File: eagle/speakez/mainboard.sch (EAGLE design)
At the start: 39 parts, among them U1 +12v

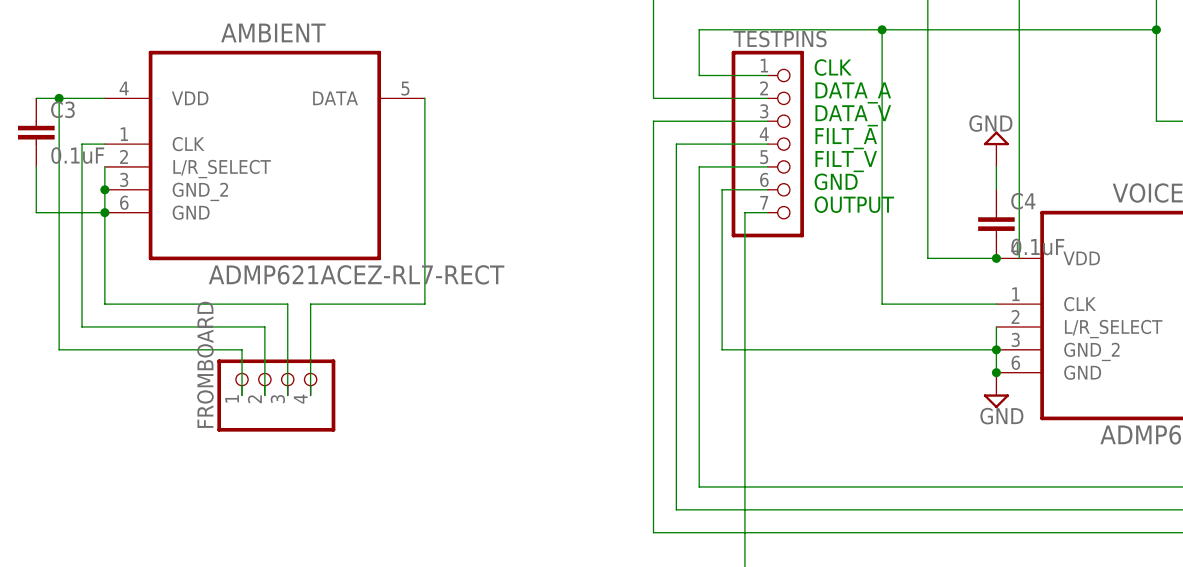
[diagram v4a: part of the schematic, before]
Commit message: started working on removing overlaps/clearance issues
still many more to go :grin:
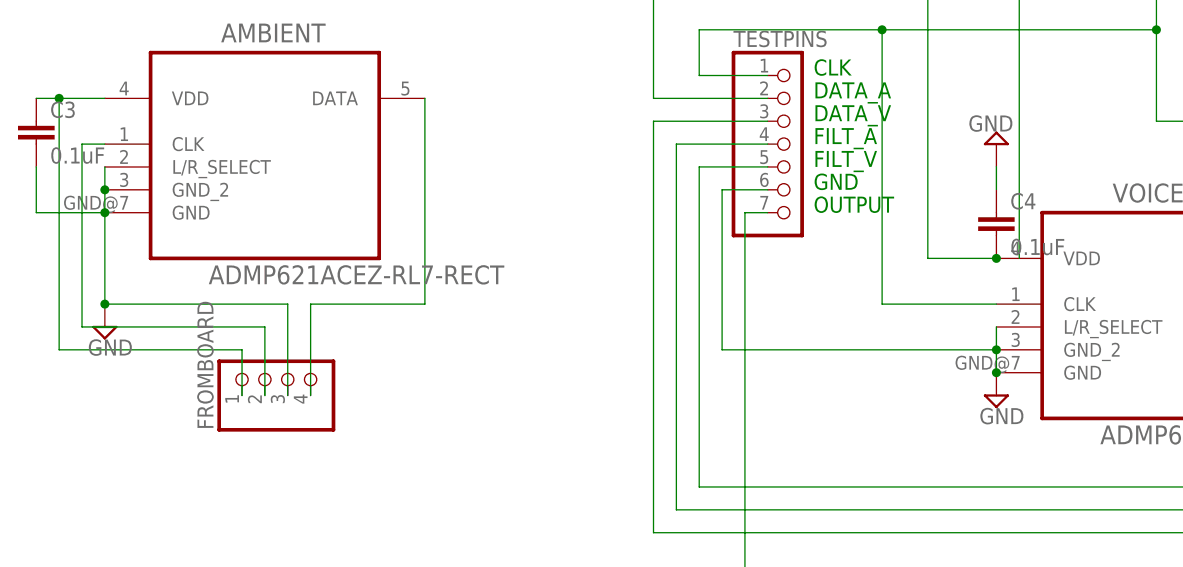
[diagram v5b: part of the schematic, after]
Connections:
- removed net N$5: AMBIENT.GND, AMBIENT.GND_2, AMBIENT.L/R_SELECT, C3.2, FROMBOARD.3
- net GND: now also AMBIENT.GND, AMBIENT.GND_2, AMBIENT.L/R_SELECT, C3.2, FROMBOARD.3
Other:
- moved on the sheet: AMBIENT, VOICE
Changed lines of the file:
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@@
 <part name="P+1" library="supply1" deviceset="+5V" device=""/>
 <part name="P+2" library="supply1" deviceset="+5V" device=""/>
+<part name="SUPPLY11" library="supply2" deviceset="GND" device=""/>
 </parts>
 <sheets>
@@
 <instance part="P+1" gate="1" x="114.3" y="111.76"/>
 <instance part="P+2" gate="1" x="243.84" y="-43.18"/>
+<instance part="SUPPLY11" gate="GND" x="-86.36" y="22.86"/>
 </instances>
 <busses>
@@
 <wire x1="236.22" y1="27.94" x2="236.22" y2="20.32" width="0.1524" layer="91"/>
 </segment>
+<segment>
+<pinref part="AMBIENT" gate="A" pin="GND"/>
+<pinref part="AMBIENT" gate="A" pin="L/R_SELECT"/>
+<pinref part="AMBIENT" gate="A" pin="GND_2"/>
+<wire x1="-86.36" y1="40.64" x2="-86.36" y2="38.1" width="0.1524" layer="91"/>
+<wire x1="-86.36" y1="38.1" x2="-86.36" y2="35.56" width="0.1524" layer="91"/>
+<junction x="-86.36" y="38.1"/>
+<wire x1="-86.36" y1="35.56" x2="-86.36" y2="25.4" width="0.1524" layer="91"/>
+<junction x="-86.36" y="35.56"/>
+<pinref part="FROMBOARD" gate="A" pin="3"/>
+<wire x1="-86.36" y1="25.4" x2="-66.04" y2="25.4" width="0.1524" layer="91"/>
+<wire x1="-66.04" y1="25.4" x2="-66.04" y2="15.24" width="0.1524" layer="91"/>
+<wire x1="-86.36" y1="35.56" x2="-93.98" y2="35.56" width="0.1524" layer="91"/>
+<pinref part="C3" gate="G$1" pin="2"/>
+<wire x1="-93.98" y1="35.56" x2="-93.98" y2="40.64" width="0.1524" layer="91"/>
+<pinref part="SUPPLY11" gate="GND" pin="GND"/>
+<junction x="-86.36" y="25.4"/>
+</segment>
 </net>
 <net name="DATA" class="0">
@@
 </segment>
 </net>
-<net name="N$5" class="0">
-<segment>
-<pinref part="AMBIENT" gate="A" pin="GND"/>
-<pinref part="AMBIENT" gate="A" pin="L/R_SELECT"/>
-<pinref part="AMBIENT" gate="A" pin="GND_2"/>
-<wire x1="-86.36" y1="40.64" x2="-86.36" y2="38.1" width="0.1524" layer="91"/>
-<wire x1="-86.36" y1="38.1" x2="-86.36" y2="35.56" width="0.1524" layer="91"/>
-<junction x="-86.36" y="38.1"/>
-<wire x1="-86.36" y1="35.56" x2="-86.36" y2="25.4" width="0.1524" layer="91"/>
-<junction x="-86.36" y="35.56"/>
-<pinref part="FROMBOARD" gate="A" pin="3"/>
-<wire x1="-86.36" y1="25.4" x2="-66.04" y2="25.4" width="0.1524" layer="91"/>
-<wire x1="-66.04" y1="25.4" x2="-66.04" y2="15.24" width="0.1524" layer="91"/>
-<wire x1="-86.36" y1="35.56" x2="-93.98" y2="35.56" width="0.1524" layer="91"/>
-<pinref part="C3" gate="G$1" pin="2"/>
-<wire x1="-93.98" y1="35.56" x2="-93.98" y2="40.64" width="0.1524" layer="91"/>
-</segment>
-</net>

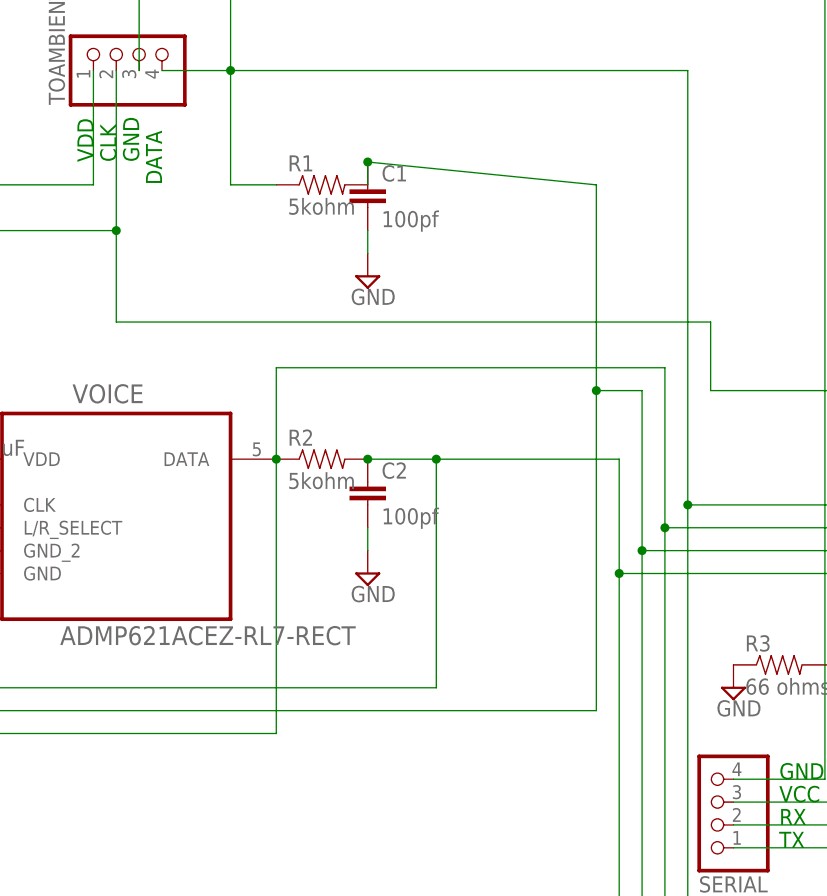
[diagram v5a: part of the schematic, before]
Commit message: fixed lots of clearance issues, added headers for filter testing
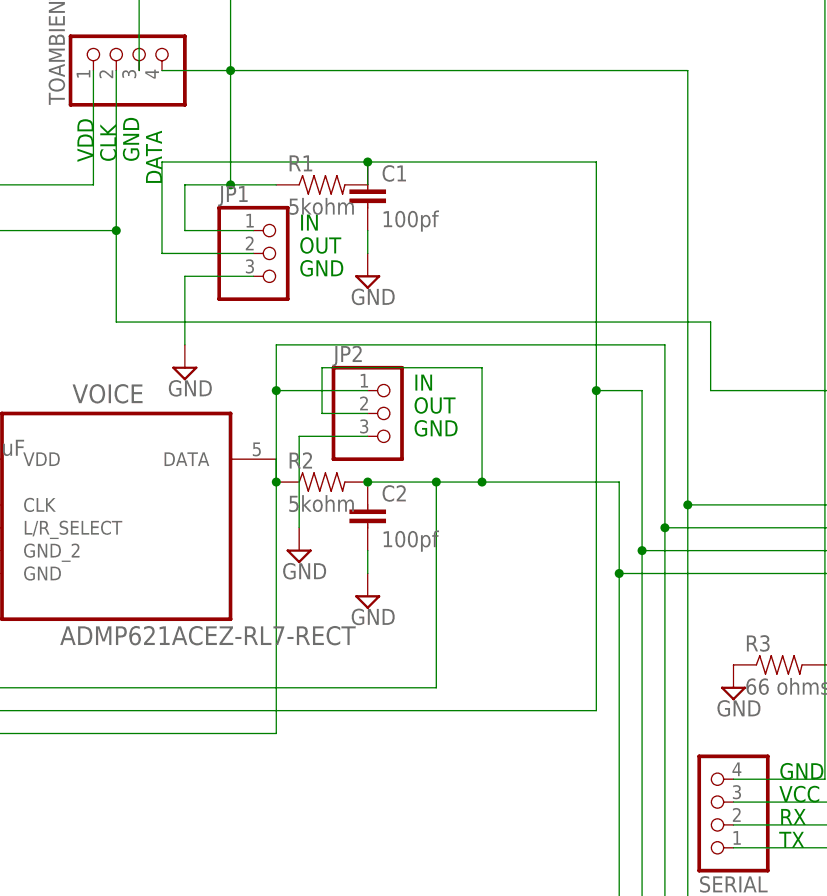
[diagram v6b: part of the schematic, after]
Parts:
- added JP1, JP2: (no value), pinhead:PINHD-1X3
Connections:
- net DATA: now also JP2.1
- net GND: now also JP1.3, JP2.3
- net N$1: now also JP1.2
- net N$10: now also JP1.1
- net N$2: now also JP2.2
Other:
- note added: "IN"
- note added: "OUT"
- moved on the sheet: C2, R2
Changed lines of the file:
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@@
 <part name="P+2" library="supply1" deviceset="+5V" device=""/>
 <part name="SUPPLY11" library="supply2" deviceset="GND" device=""/>
+<part name="JP1" library="pinhead" deviceset="PINHD-1X3" device=""/>
+<part name="JP2" library="pinhead" deviceset="PINHD-1X3" device=""/>
+<part name="SUPPLY12" library="supply2" deviceset="GND" device=""/>
+<part name="SUPPLY13" library="supply2" deviceset="GND" device=""/>
 </parts>
 <sheets>
@@
 <text x="223.52" y="-33.02" size="1.778" layer="91">J-LINK RX</text>
 <text x="198.12" y="-38.1" size="1.778" layer="91">jtag_trst</text>
+<text x="50.8" y="55.88" size="1.778" layer="91">IN</text>
+<text x="50.8" y="53.34" size="1.778" layer="91">OUT</text>
+<text x="50.8" y="50.8" size="1.778" layer="91">GND</text>
+<text x="63.5" y="33.02" size="1.778" layer="91">GND</text>
+<text x="63.5" y="35.56" size="1.778" layer="91">OUT</text>
+<text x="63.5" y="38.1" size="1.778" layer="91">IN</text>
 </plain>
 <instances>
 <instance part="R1" gate="G$1" x="53.34" y="60.96"/>
-<instance part="R2" gate="G$1" x="53.34" y="30.48"/>
+<instance part="R2" gate="G$1" x="53.34" y="27.94"/>
 <instance part="C1" gate="G$1" x="58.42" y="58.42"/>
-<instance part="C2" gate="G$1" x="58.42" y="25.4"/>
+<instance part="C2" gate="G$1" x="58.42" y="22.86"/>
 <instance part="SUPPLY1" gate="GND" x="58.42" y="50.8"/>
-<instance part="SUPPLY2" gate="GND" x="58.42" y="17.78"/>
+<instance part="SUPPLY2" gate="GND" x="58.42" y="15.24"/>
 <instance part="AMBIENT" gate="A" x="-68.58" y="45.72"/>
 <instance part="VOICE" gate="A" x="30.48" y="27.94"/>
@@
 <instance part="P+2" gate="1" x="243.84" y="-43.18"/>
 <instance part="SUPPLY11" gate="GND" x="-86.36" y="22.86"/>
+<instance part="JP1" gate="A" x="48.26" y="53.34"/>
+<instance part="JP2" gate="A" x="60.96" y="35.56"/>
+<instance part="SUPPLY12" gate="GND" x="50.8" y="20.32"/>
+<instance part="SUPPLY13" gate="GND" x="38.1" y="40.64"/>
 </instances>
 <busses>
@@
 <pinref part="R1" gate="G$1" pin="2"/>
 <pinref part="C1" gate="G$1" pin="1"/>
-<wire x1="58.42" y1="63.5" x2="83.82" y2="60.96" width="0.1524" layer="91"/>
+<wire x1="58.42" y1="63.5" x2="83.82" y2="63.5" width="0.1524" layer="91"/>
 <junction x="58.42" y="63.5"/>
-<wire x1="83.82" y1="60.96" x2="83.82" y2="38.1" width="0.1524" layer="91"/>
+<wire x1="83.82" y1="63.5" x2="83.82" y2="38.1" width="0.1524" layer="91"/>
 <wire x1="83.82" y1="38.1" x2="83.82" y2="2.54" width="0.1524" layer="91"/>
 <wire x1="83.82" y1="2.54" x2="-22.86" y2="2.54" width="0.1524" layer="91"/>
@@
 <wire x1="-22.86" y1="43.18" x2="-12.7" y2="43.18" width="0.1524" layer="91"/>
 <wire x1="58.42" y1="60.96" x2="58.42" y2="63.5" width="0.1524" layer="91"/>
+<pinref part="JP1" gate="A" pin="2"/>
+<wire x1="45.72" y1="53.34" x2="35.56" y2="53.34" width="0.1524" layer="91"/>
+<wire x1="35.56" y1="53.34" x2="35.56" y2="63.5" width="0.1524" layer="91"/>
+<wire x1="35.56" y1="63.5" x2="58.42" y2="63.5" width="0.1524" layer="91"/>
 </segment>
 </net>
@@
 <pinref part="R2" gate="G$1" pin="2"/>
 <pinref part="C2" gate="G$1" pin="1"/>
-<wire x1="58.42" y1="30.48" x2="66.04" y2="30.48" width="0.1524" layer="91"/>
-<wire x1="66.04" y1="30.48" x2="66.04" y2="5.08" width="0.1524" layer="91"/>
-<junction x="58.42" y="30.48"/>
+<wire x1="58.42" y1="27.94" x2="66.04" y2="27.94" width="0.1524" layer="91"/>
+<wire x1="66.04" y1="27.94" x2="66.04" y2="5.08" width="0.1524" layer="91"/>
+<junction x="58.42" y="27.94"/>
 <wire x1="-20.32" y1="40.64" x2="-20.32" y2="5.08" width="0.1524" layer="91"/>
 <wire x1="-20.32" y1="5.08" x2="66.04" y2="5.08" width="0.1524" layer="91"/>
-<wire x1="86.36" y1="17.78" x2="86.36" y2="30.48" width="0.1524" layer="91"/>
-<wire x1="86.36" y1="30.48" x2="66.04" y2="30.48" width="0.1524" layer="91"/>
-<junction x="66.04" y="30.48"/>
+<wire x1="86.36" y1="17.78" x2="86.36" y2="27.94" width="0.1524" layer="91"/>
+<wire x1="86.36" y1="27.94" x2="71.12" y2="27.94" width="0.1524" layer="91"/>
+<junction x="66.04" y="27.94"/>
 <pinref part="U$1" gate="G$1" pin="D19/A5/SCL0/TOUCH"/>
+<wire x1="71.12" y1="27.94" x2="66.04" y2="27.94" width="0.1524" layer="91"/>
 <wire x1="116.84" y1="17.78" x2="86.36" y2="17.78" width="0.1524" layer="91"/>
 <wire x1="86.36" y1="17.78" x2="86.36" y2="-27.94" width="0.1524" layer="91"/>
@@
 <pinref part="TESTPINS" gate="A" pin="5"/>
 <wire x1="-20.32" y1="40.64" x2="-12.7" y2="40.64" width="0.1524" layer="91"/>
+<pinref part="JP2" gate="A" pin="2"/>
+<wire x1="58.42" y1="35.56" x2="53.34" y2="35.56" width="0.1524" layer="91"/>
+<wire x1="53.34" y1="35.56" x2="53.34" y2="40.64" width="0.1524" layer="91"/>
+<wire x1="53.34" y1="40.64" x2="71.12" y2="40.64" width="0.1524" layer="91"/>
+<wire x1="71.12" y1="40.64" x2="71.12" y2="27.94" width="0.1524" layer="91"/>
+<junction x="71.12" y="27.94"/>
 </segment>
 </net>
@@
 <pinref part="C2" gate="G$1" pin="2"/>
 <pinref part="SUPPLY2" gate="GND" pin="GND"/>
-<wire x1="58.42" y1="20.32" x2="58.42" y2="22.86" width="0.1524" layer="91"/>
+<wire x1="58.42" y1="17.78" x2="58.42" y2="20.32" width="0.1524" layer="91"/>
 </segment>
 <segment>
@@
 <junction x="-86.36" y="25.4"/>
 </segment>
+<segment>
+<pinref part="JP2" gate="A" pin="3"/>
+<wire x1="58.42" y1="33.02" x2="50.8" y2="33.02" width="0.1524" layer="91"/>
+<wire x1="50.8" y1="33.02" x2="50.8" y2="22.86" width="0.1524" layer="91"/>
+<pinref part="SUPPLY12" gate="GND" pin="GND"/>
+</segment>
+<segment>
+<pinref part="JP1" gate="A" pin="3"/>
+<pinref part="SUPPLY13" gate="GND" pin="GND"/>
+<wire x1="45.72" y1="50.8" x2="38.1" y2="50.8" width="0.1524" layer="91"/>
+<wire x1="38.1" y1="50.8" x2="38.1" y2="43.18" width="0.1524" layer="91"/>
+</segment>
 </net>
 <net name="DATA" class="0">
@@
 <pinref part="VOICE" gate="A" pin="DATA"/>
 <pinref part="R2" gate="G$1" pin="1"/>
-<wire x1="48.26" y1="30.48" x2="48.26" y2="0" width="0.1524" layer="91"/>
-<junction x="48.26" y="30.48"/>
+<wire x1="48.26" y1="27.94" x2="48.26" y2="0" width="0.1524" layer="91"/>
+<junction x="48.26" y="27.94"/>
 <wire x1="48.26" y1="0" x2="-25.4" y2="0" width="0.1524" layer="91"/>
 <wire x1="-25.4" y1="0" x2="-25.4" y2="45.72" width="0.1524" layer="91"/>
-<wire x1="91.44" y1="22.86" x2="91.44" y2="40.64" width="0.1524" layer="91"/>
-<wire x1="91.44" y1="40.64" x2="48.26" y2="40.64" width="0.1524" layer="91"/>
-<wire x1="48.26" y1="40.64" x2="48.26" y2="30.48" width="0.1524" layer="91"/>
+<wire x1="91.44" y1="22.86" x2="91.44" y2="43.18" width="0.1524" layer="91"/>
+<wire x1="91.44" y1="43.18" x2="48.26" y2="43.18" width="0.1524" layer="91"/>
+<wire x1="48.26" y1="43.18" x2="48.26" y2="38.1" width="0.1524" layer="91"/>
 <pinref part="U$1" gate="G$1" pin="D17/A3/TOUCH"/>
+<wire x1="48.26" y1="38.1" x2="48.26" y2="27.94" width="0.1524" layer="91"/>
 <wire x1="116.84" y1="22.86" x2="91.44" y2="22.86" width="0.1524" layer="91"/>
 <wire x1="91.44" y1="22.86" x2="91.44" y2="-22.86" width="0.1524" layer="91"/>
@@
 <pinref part="TESTPINS" gate="A" pin="3"/>
 <wire x1="-25.4" y1="45.72" x2="-12.7" y2="45.72" width="0.1524" layer="91"/>
+<wire x1="48.26" y1="27.94" x2="48.26" y2="30.48" width="0.1524" layer="91"/>
+<pinref part="JP2" gate="A" pin="1"/>
+<wire x1="48.26" y1="38.1" x2="58.42" y2="38.1" width="0.1524" layer="91"/>
+<junction x="48.26" y="38.1"/>
 </segment>
 </net>
@@
 <pinref part="TESTPINS" gate="A" pin="2"/>
 <wire x1="-25.4" y1="48.26" x2="-12.7" y2="48.26" width="0.1524" layer="91"/>
-</segment>
-</net>
+<wire x1="43.18" y1="60.96" x2="38.1" y2="60.96" width="0.1524" layer="91"/>
+<junction x="43.18" y="60.96"/>
+<wire x1="38.1" y1="60.96" x2="38.1" y2="55.88" width="0.1524" layer="91"/>
+<pinref part="JP1" gate="A" pin="1"/>
+<wire x1="38.1" y1="55.88" x2="45.72" y2="55.88" width="0.1524" layer="91"/>
+</segment>
+</net>
